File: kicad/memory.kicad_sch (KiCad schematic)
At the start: 13 parts, among them J8 Molex 87715-9106, U11 ATF22V10C-7PX, U12 ATF22V10C-7PX, U25 CD74ACT273E, U31 AS7C256C-15PCN, U32 AS7C256C-15PCN

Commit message: Put every symbol, footprint and 3D model in the project library
- gen_kicad_stock_footprints.py: copies of the KiCad 9.0.6 footprints the
  boards use (C_Disc, CP_Radial, DO-15/DO-35, LED, pin header, oscillator,
  TO-92, SIP9, mounting holes, net tie) into placard.pretty, and KiCad's
  STEP models for them and for the DIP socket / resistor kit footprints
  into placard.3dshapes
- model paths use the PLACARD_LIB text variable (main board
  ${KIPRJMOD}/lib, cartridges ${KIPRJMOD}/../lib) so the shared footprints
  find their models in all three projects
- placard_std gains the 28C256 EEPROM and the power symbols; symbol
  Footprint defaults name placard footprints (relay, SIP9, oscillator,
  TO-92, EEPROM socket)
- schematics regenerated with placard_std power/EEPROM symbols and
  placard: footprints; BOM CSVs and PDFs regenerated
- cartridge .kicad_pro files take in Justin's local KiCad 9 settings

Co-Authored-By: Claude Opus 5.5 <noreply@anthropic.com>
Claude-Session: https://claude.ai/code/session_017okF1JiLRNFTfH7Az85hff
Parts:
- C11, C12, C25, C31, C32: footprint Capacitor_THT:C_Disc_D5.0mm_W2.5mm_P5.00mm -> placard:C_Disc_D5.0mm_W2.5mm_P5.00mm

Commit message: Schematic: rename buses to ADDR / DATABUS / D, wire the shared port outputs
- Address bus A15:A0 is now ADDR15:ADDR0, the data bus D7:D0 is DATABUS7:DATABUS0
  and the D register's outputs DR7:DR0 are D7:D0 (main board and both cartridges).
- Shared port sheet: U38's outputs P_SCK, P_MOSI, P_CS, P_PS2D and K0 are wired
  to the SNES pads, the SD dividers and the PS/2 hold diodes (K0 -> D6 ->
  keyboard CLK).  J3 now sits level with U38's SCK/MOSI pins, J2 above it.
- Parts moved so the longer labels fit: U3/U4 and the PC bus, U18, U22, U11,
  U31, U32, RN1, R5-R12; expansion slots in two rows.
- SCHEMATIC_PLAN.md: the bus names.

Co-Authored-By: Claude Opus 5.5 <noreply@anthropic.com>
Claude-Session: https://claude.ai/code/session_01DnW5SUv7E4nz9tGtPvD1qV
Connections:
- net A0 renamed ADDR0
- net A1 renamed ADDR1
- net A10 renamed ADDR10
- net A11 renamed ADDR11
- net A12 renamed ADDR12
- net A13 renamed ADDR13
- net A14 renamed ADDR14
- net A15 renamed ADDR15
- net A2 renamed ADDR2
- net A3 renamed ADDR3
- net A4 renamed ADDR4
- net A5 renamed ADDR5
- net A6 renamed ADDR6
- net A7 renamed ADDR7
- net A8 renamed ADDR8
- net A9 renamed ADDR9
- net D0 renamed DATABUS0
- net D1 renamed DATABUS1
- net D2 renamed DATABUS2
- net D3 renamed DATABUS3
- net D4 renamed DATABUS4
- net D5 renamed DATABUS5
- net D6 renamed DATABUS6
- net D7 renamed DATABUS7
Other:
- moved on the sheet: C11, C31, C32, U11, U31, U32

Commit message: Option B: muxes take the enables as selects, /WE from an early clock tap
Removes the Sync PLD pass from every memory address (docs/FETCH_TIMING.md):
the instruction fetch gains 8.2 ns, X/Y/video/upper-32K reads 9.7 ns, the
zero-page store start 6.9 ns, and the address hold after /WE is +0.5 ns
from the datasheets alone.  No new parts, no extra clock, no PLCC.

- ATF22V10_QUAD_MUX.pld rev 02: two low + two high address bits per chip,
  PIXEL_ENABLE / PC_ENABLE / X_ENABLE / Y_ENABLE as the selects
- ATF22V10_SYNC.pld rev 10: ADDR_SEL outputs gone; /WE on pin 20 from the
  early clock tap CLK_E (pin 9), RW and RUN inputs, OE = RUN
- ATF22V10_MEM_CTRL.pld rev 10: /WE gone (pin 16 free)
- ATF22V10_IO_DECODE.pld rev 05: /CE_HI from the enables, RW dropped
- FPGA model and benches follow; GHDL: tb_cart_load (2 seeds), tb_top_load,
  tb_blank_line pass, and cpu_test makes the same 69,776 RAM writes as main
- Schematic: mux sheet rewired, /WE from U15, net tie NT2 between CLK_E and
  CLK on the power sheet (the 500 mm of track), symbols regenerated, PDFs
- Docs updated; docs/option_b_board.png shows the board rewiring (no chip
  has to move)

Co-Authored-By: Claude Fable 5.1 <noreply@anthropic.com>
Claude-Session: https://claude.ai/code/session_01DnW5SSBUc8XDbr4GrYdwj8
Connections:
- net ADDR_SEL is gone; now on net PIXEL_ENABLE: U12.2 (PIXEL_ENABLE)
- net ADDR_SEL_HI is gone; now on net PC_ENABLE: U12.3 (PC_ENABLE)
- net RW: no longer U12.14 (RW)
- net ~{WE}: no longer U11.16 (/WE)
- new net Y_ENABLE: U12.14 (Y_ENABLE)
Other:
- note added: "/WE comes from U15 (Sync, sheet 8). RUN low (cartridge loading): /ROM_OE held off, map register clear (all ROM), /WE let go (R63)."
- note removed: "RUN low (cartridge loading): /ROM_OE held off, map register clear (all ROM), /WE let go (R63)."

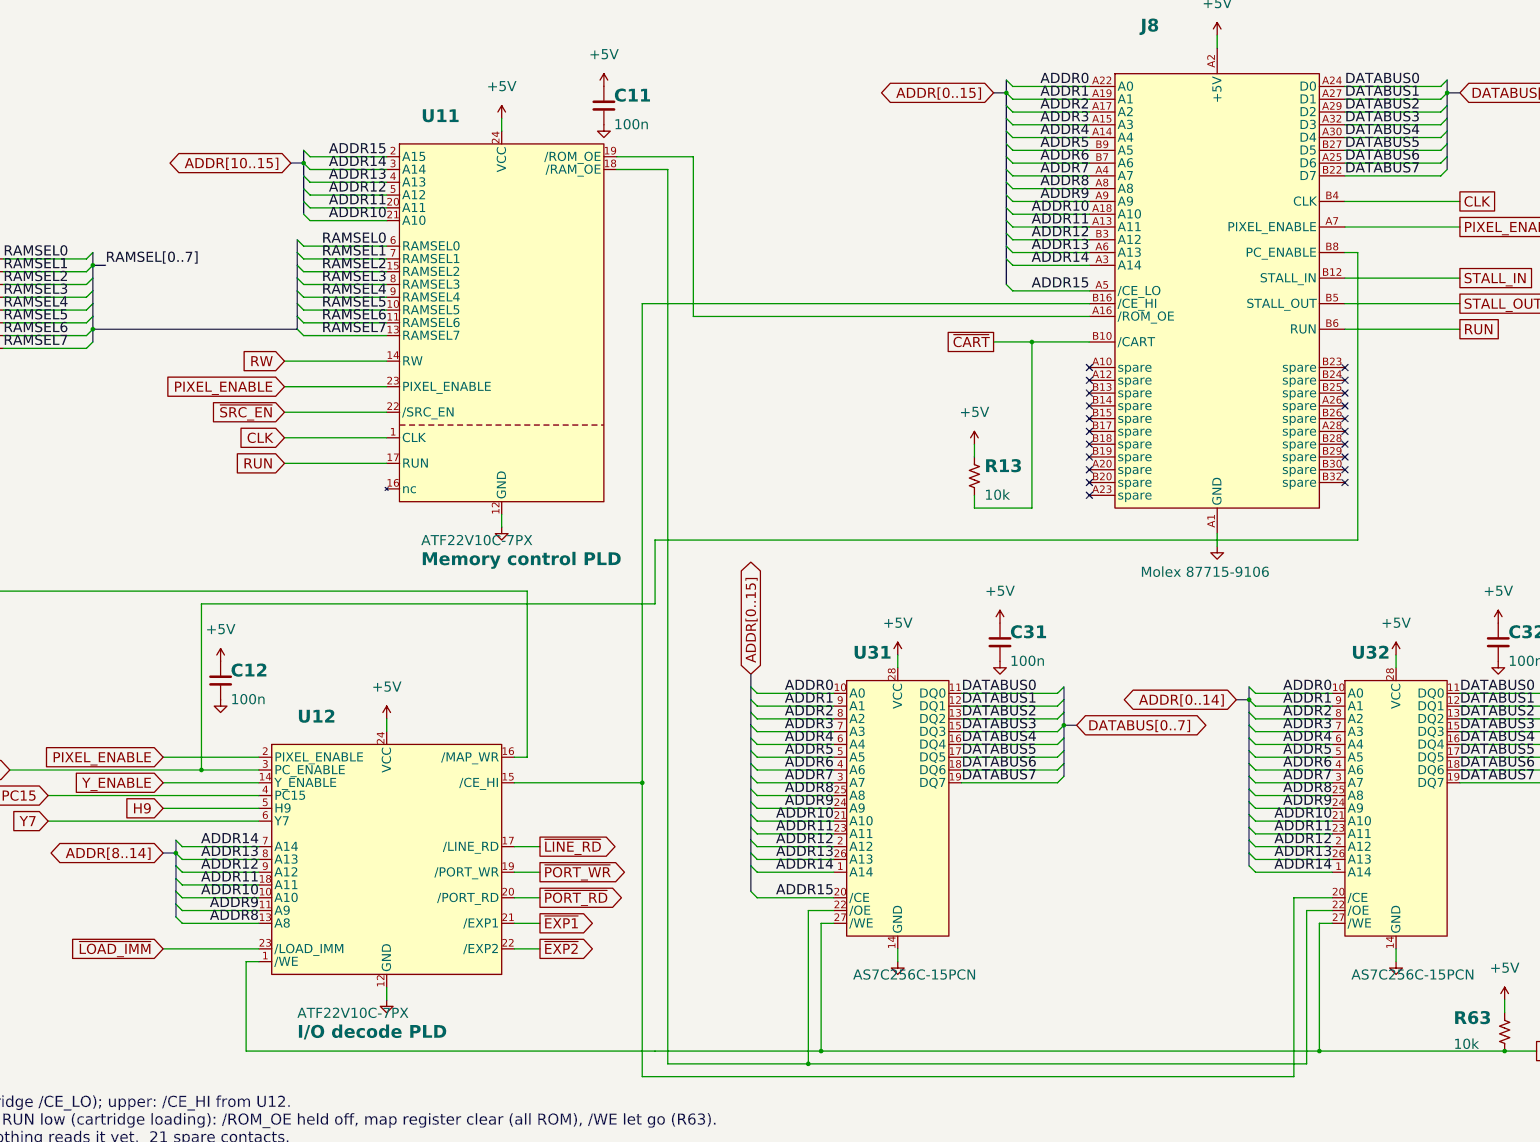
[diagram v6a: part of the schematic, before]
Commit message: Expansion slots: grounds on the inner rows, signals outer; take in Justin's KiCad edits
Reassign the expansion slot contacts so the extra grounds sit on the
inner (even) rows and the signals on the outer (odd) rows wherever the
cartridge pinout allows: 19 of 38 signals outer.  The cartridge's power
and ground contacts, the shared signals and the wrong-slot rules are
kept (every expansion output and extra ground on a J8 spare, every
cartridge output open on the expansion slot).  BT4 and BT6-BT8 dropped.

Justin's local KiCad edits (all main-board sheets, the board and the
project; K1 coil pins swapped) are committed as he saved them; only the
expansion sheet comes from the generator.  Netlist differs from his
only on J9-J12; ERC unchanged.

Co-Authored-By: Claude Opus 5.5 <noreply@anthropic.com>
Claude-Session: https://claude.ai/code/session_01DnW5SUDtmC2C2nXUS4xVk2
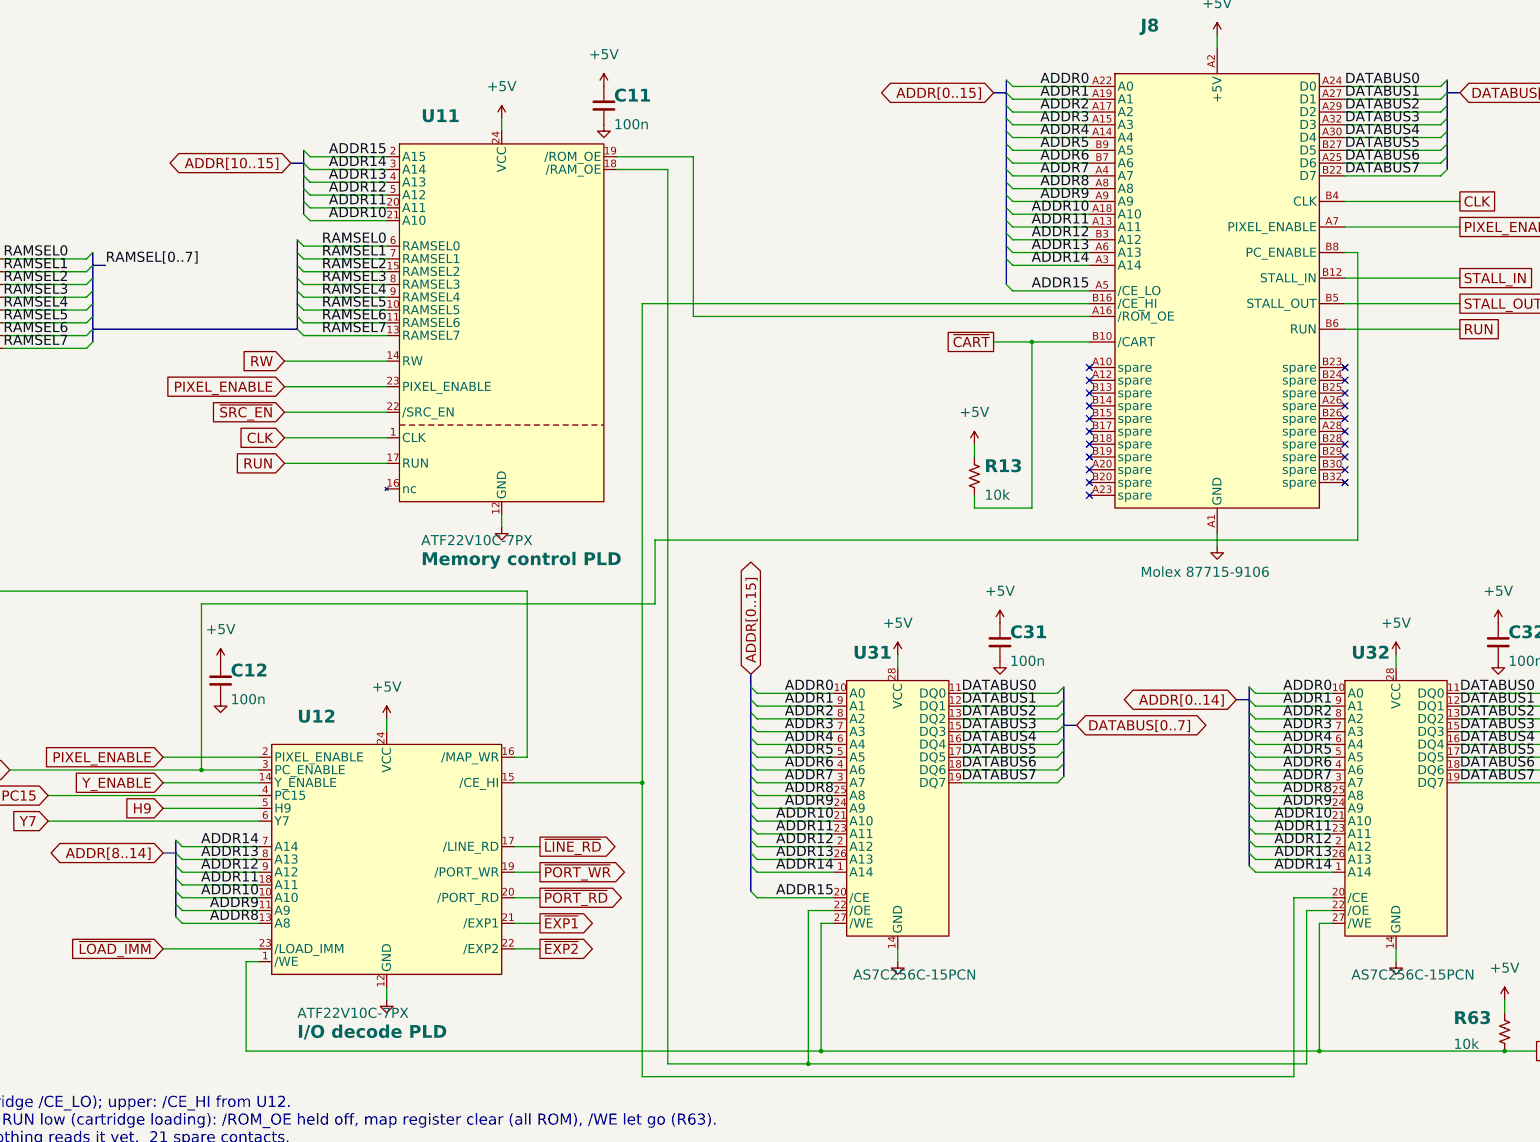
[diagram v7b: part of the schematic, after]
